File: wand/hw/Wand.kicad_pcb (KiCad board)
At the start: 2 copper layers, 0 parts

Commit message: (WIP) Wand PCB design
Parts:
- added AE1: 2.4GHz 50R, Wand_footprints:ANT_IFA_USB_2.4GHz_50R, F.Cu at (72.2, 25.4)
- added BT1: LiPo, Wand_footprints:Pads_1x02_P2.5, F.Cu at (37.8, 26.1)
- added C1: 10n, Capacitor_SMD:C_0603_1608Metric, F.Cu at (43.4, 31.7)
- added C10: 10n, Capacitor_SMD:C_0402_1005Metric, F.Cu at (61.0, 33.6)
- added C11: 10n, Capacitor_SMD:C_0402_1005Metric, F.Cu at (62.2, 27.0)
- added C12: 33n, Capacitor_SMD:C_0402_1005Metric, F.Cu at (60.4, 26.5)
- added C13: 10p, Capacitor_SMD:C_0402_1005Metric, F.Cu at (64.5, 36.2)
- added C14: 10p, Capacitor_SMD:C_0402_1005Metric, F.Cu at (60.5, 37.2)
- added C15: 1.5p, Capacitor_SMD:C_0402_1005Metric, F.Cu at (68.8, 29.8)
- added C16: 1p, Capacitor_SMD:C_0402_1005Metric, F.Cu at (69.2, 28.4)
- added C17: 2.2n, Capacitor_SMD:C_0402_1005Metric, F.Cu at (68.1, 31.9)
- added C18: 4.7p, Capacitor_SMD:C_0402_1005Metric, F.Cu at (68.1, 30.9)
- added C19: 4.7u, Capacitor_SMD:C_0603_1608Metric, F.Cu at (33.0, 27.6)
- added C2: 4.7u, Capacitor_SMD:C_0603_1608Metric, F.Cu at (46.3, 29.1)
- added C20: 10u, Capacitor_SMD:C_0603_1608Metric, F.Cu at (37.0, 29.5)
- added C3: 4.7u, Capacitor_SMD:C_0603_1608Metric, F.Cu at (47.8, 29.6)
- added C4: 100n, Capacitor_SMD:C_0603_1608Metric, F.Cu at (49.3, 29.6)
- added C5: 100n, Capacitor_SMD:C_0402_1005Metric, F.Cu at (48.7, 45.7)
- added C6: 100n, Capacitor_SMD:C_0402_1005Metric, F.Cu at (51.4, 46.1)
- added C7: 2.2u, Capacitor_SMD:C_0402_1005Metric, F.Cu at (53.2, 46.1)
- added C8: 1n, Capacitor_SMD:C_0603_1608Metric, B.Cu at (42.0, 28.6)
- added C9: 4.7u, Capacitor_SMD:C_0402_1005Metric, F.Cu at (62.2, 26.0)
- added D1: SMBJ5.0A, Diode_SMD:D_SMB, F.Cu at (26.9, 37.4)
- added D2: LED, LED_SMD:LED_0603_1608Metric, F.Cu at (36.7, 34.1)
- added J1: Conn_01x04, Wand_footprints:TestPoints_1x04_P2.0, F.Cu at (52.1, 25.7)
- added J2: Conn_01x08, Connector_PinHeader_1.00mm:PinHeader_1x08_P1.00mm_Vertical, F.Cu at (53.4, 39.0)
- added J3: Conn_01x08, Connector_PinHeader_1.00mm:PinHeader_1x08_P1.00mm_Vertical, F.Cu at (53.4, 41.2)
- added J4: Conn_01x04, Connector_PinHeader_1.00mm:PinHeader_1x04_P1.00mm_Vertical, F.Cu at (46.4, 46.0)
- added J5: USB_C_Receptacle_PowerOnly_6P, Wand_footprints:USB_C_Receptacle, F.Cu at (27.4, 29.8)
- added L1: 8.2n, Capacitor_SMD:C_0402_1005Metric, F.Cu at (65.3, 30.3)
- added L2: 2.7n, Capacitor_SMD:C_0402_1005Metric, F.Cu at (66.4, 31.4)
- added L3: 3.9n, Capacitor_SMD:C_0402_1005Metric, F.Cu at (66.9, 29.8)
- added M1: Motor_DC, Wand_footprints:Pads_1x02_P2.5, B.Cu at (57.0, 37.3)
- added Q1: Si2301, Package_TO_SOT_SMD:SOT-23, F.Cu at (55.5, 36.7)
- added Q2: Si2301, Package_TO_SOT_SMD:SOT-23, B.Cu at (55.9, 34.7)
- added R1: 1.2M, Resistor_SMD:R_0603_1608Metric, F.Cu at (57.6, 25.8)
- added R10: 1k, Resistor_SMD:R_0603_1608Metric, B.Cu at (58.6, 34.6)
- added R11: 5.1k, Resistor_SMD:R_0603_1608Metric, F.Cu at (32.0, 36.4)
- added R12: 5.1k, Resistor_SMD:R_0603_1608Metric, F.Cu at (32.0, 37.9)
- added R13: 2k, Resistor_SMD:R_0603_1608Metric, F.Cu at (33.7, 32.5)
- added R14: 6.8k, Resistor_SMD:R_0603_1608Metric, F.Cu at (33.7, 34.1)
- added R2: 1k, Resistor_SMD:R_0603_1608Metric, F.Cu at (51.4, 36.6)
- added R3: 1k, Resistor_SMD:R_0603_1608Metric, F.Cu at (52.9, 36.6)
- added R4: 1k TBD, Resistor_SMD:R_0603_1608Metric, F.Cu at (46.1, 36.6)
- added R5: 1k TBD, Resistor_SMD:R_0603_1608Metric, F.Cu at (47.6, 36.6)
- added R6: 1k TBD, Resistor_SMD:R_0603_1608Metric, F.Cu at (49.1, 36.6)
- added R7: 3.3M, Resistor_SMD:R_0603_1608Metric, B.Cu at (43.6, 28.6)
- added R8: 100k, Resistor_SMD:R_0603_1608Metric, B.Cu at (42.9, 34.6)
- added R9: 22k, Resistor_SMD:R_0603_1608Metric, F.Cu at (65.3, 26.7)
- added SW1: SW_SPST, Wand_footprints:SPST_1x01_P2.54, F.Cu at (40.0, 33.0)
- added SW2: Vib, Wand_footprints:VibSwitch_JYX-1210-X160, B.Cu at (42.9, 32.0)
- added U1: SPX3819M5-L-3-3, Package_TO_SOT_SMD:SOT-23-5, F.Cu at (43.4, 29.1)
- added U2: STM32G030F6Px, Package_SO:TSSOP-20_4.4x6.5mm_P0.65mm, F.Cu at (53.9, 30.4)
- added U3: BMI270, Wand_footprints:QFN50P300X250X87-14N, F.Cu at (52.1, 43.8)
- added U4: MMC5603NJ, Package_BGA:WLP-4_0.86x0.86mm_P0.4mm, F.Cu at (48.6, 43.8)
- added U5: nRF24L01P, Wand_footprints:QFN-20-P0.5, F.Cu at (62.0, 30.1)
- added U6: LTC4054ES5-4.2, Package_TO_SOT_SMD:TSOT-23-5, F.Cu at (34.1, 30.1)
- added Y1: 16MHz, Crystal:Crystal_SMD_2016-4Pin_2.0x1.6mm, F.Cu at (62.5, 36.4)
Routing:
- net VDD: track 0.00 -> 44.3 mm, vias 0 -> 2
- net GND: track 0.00 -> 38.0 mm, vias 0 -> 35
- net VBUS: track 0.00 -> 24.6 mm
- net VDDSUB: track 0.00 -> 22.3 mm, vias 0 -> 1
- net VIB_TRG: track 0.00 -> 20.7 mm, vias 0 -> 1
- net Net-(SW1-B): track 0.00 -> 15.2 mm
- net SPI2_SCK: track 0.00 -> 15.2 mm, vias 0 -> 1
- net Net-(U2-PB3/PB4/PB5/PB6): track 0.00 -> 14.5 mm, vias 0 -> 2
- net Net-(U2-PB0/PB1/PB2/PA8): track 0.00 -> 13.9 mm, vias 0 -> 2
- net BMI_CS: track 0.00 -> 13.6 mm, vias 0 -> 1
- net VBAT: track 0.00 -> 12.3 mm, vias 0 -> 1
- net Net-(U2-PB7/PB8): track 0.00 -> 12.1 mm, vias 0 -> 2
- net SUB_VDD_G: track 0.00 -> 10.4 mm, vias 0 -> 2
- net Net-(U2-PA12/PA10): track 0.00 -> 10.2 mm
- net Net-(J5-CC1): track 0.00 -> 10.00 mm
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- added copper zone on B.Cu, net GND
- added copper zone on F.Cu, net GND
- added copper zone on B.Cu, net VIB_TRG
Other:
- board outline added: 55 x 22.1 mm

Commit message: Revise wand hardware design
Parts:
- M1: moved to F.Cu
- moved M1 14.0 mm to (43.1, 38.2)
- moved Q2 14.0 mm to (42.0, 35.6)
- moved R10 14.0 mm to (44.7, 35.5)
- moved SW2 2.07 mm to (43.1, 29.9)
- moved C8 2.07 mm to (42.3, 26.6)
- moved R7 2.07 mm to (43.9, 26.6)
- moved R8 2.07 mm to (43.1, 32.6)
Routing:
- net VDD: track 44.3 -> 58.4 mm, vias 2 -> 3
- net MOTOR_G: track 2.02 -> 13.4 mm
- net VIB_TRG: track 20.7 -> 19.6 mm
- net GND: track 38.0 -> 37.0 mm
- net VBAT: track 12.3 -> 13.0 mm
- net Net-(U2-PB0/PB1/PB2/PA8): track 13.9 -> 14.4 mm
- net Net-(M1--): track 3.21 -> 3.59 mm, vias 0 -> 1
- added copper zone on F.Cu, net VDD

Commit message: Revise wand hardware design
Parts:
- added G***: LOGO, LOGO, B.Cu at (75.2, 36.9)
- added G***: LOGO, LOGO, B.Cu at (74.9, 29.9)
- added G***: LOGO, LOGO, B.Cu at (25.4, 37.4)
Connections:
- Q1 pad 2: VDDSUB -> VDD
- Q1 pad 3: VDD -> VDDSUB
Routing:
- net VDDSUB: track 22.3 -> 24.7 mm
- net GND: track 37.0 -> 35.6 mm, vias 35 -> 137
- net VDD: track 58.4 -> 57.4 mm
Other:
- board text added: "23-Cold"
- board text added: "JLCJLCJLCJLC"
- board text added: "Malletwand"
- board text added: "Wand Rev. 2"

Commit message: Revise silkscreen text; submit for fabrication
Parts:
- added G***: LOGO, LOGO, B.Cu at (30.8, 38.6)
- moved G*** 0.23 mm to (75.2, 29.9)
- moved G*** 0.06 mm to (75.3, 37.0)
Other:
- board text removed: "23-Cold"

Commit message: Fix incorrect markings in ECAD files
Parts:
- C5: renamed from C7; value 2.2u -> 100n
- C7: renamed from C5; value 100n -> 2.2u
- M1: value Motor_DC -> Vib
- Q2: value Si2301 -> Si2302
- turned C5 to 180 degrees
- turned C7 to 0 degrees
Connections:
- C5 pad 1: GND -> VDDSUB
- C5 pad 2: VDDSUB -> GND
- C7 pad 1: VDDSUB -> GND
- C7 pad 2: GND -> VDDSUB
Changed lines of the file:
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@@
   )
   (footprint "Capacitor_SMD:C_0402_1005Metric" (layer "F.Cu")
-    (at 48.7 45.7 180)
+    (at 48.7 45.7)
     (descr "Capacitor SMD 0402 (1005 Metric), square (rectangular) end terminal, IPC_7351 nominal, (Body size source: IPC-SM-782 page 76, https://www.pcb-3d.com/wordpress/wp-content/uploads/ipc-sm-782a_amendment_1_and_2.pdf), generated with kicad-footprint-generator")
     (tags "capacitor")
@@
     (property "ki_keywords" "cap capacitor")
     (attr smd)
-    (fp_text reference "C5" (at 0 0 180) (layer "B.SilkS")
+    (fp_text reference "C7" (at 0 0) (layer "B.SilkS")
         (effects (font (size 0.8 0.8) (thickness 0.15)) (justify mirror))
     )
-    (fp_text value "100n" (at 0 1.16) (layer "F.Fab")
+    (fp_text value "2.2u" (at 0 1.16) (layer "F.Fab")
         (effects (font (size 1 1) (thickness 0.15)))
     )
@@
     (fp_line (start 0.5 0.25) (end -0.5 0.25)
       (stroke (width 0.1) (type solid)) (layer "F.Fab"))
-    (pad "1" smd roundrect (at -0.48 0 180) (size 0.56 0.62) (layers "F.Cu" "F.Paste" "F.Mask") (roundrect_rratio 0.25)
-      (net 43 "VDDSUB") (pintype "passive"))
-    (pad "2" smd roundrect (at 0.48 0 180) (size 0.56 0.62) (layers "F.Cu" "F.Paste" "F.Mask") (roundrect_rratio 0.25)
+    (pad "1" smd roundrect (at -0.48 0) (size 0.56 0.62) (layers "F.Cu" "F.Paste" "F.Mask") (roundrect_rratio 0.25)
       (net 2 "GND") (pintype "passive"))
+    (pad "2" smd roundrect (at 0.48 0) (size 0.56 0.62) (layers "F.Cu" "F.Paste" "F.Mask") (roundrect_rratio 0.25)
+      (net 43 "VDDSUB") (pintype "passive"))
     (model "${KICAD6_3DMODEL_DIR}/Capacitor_SMD.3dshapes/C_0402_1005Metric.wrl"
       (offset (xyz 0 0 0))
@@
         (effects (font (size 0.8 0.8) (thickness 0.15)))
     )
-    (fp_text value "Motor_DC" (at 0 1 180 unlocked) (layer "F.Fab")
+    (fp_text value "Vib" (at 0 1 180 unlocked) (layer "F.Fab")
         (effects (font (size 1 1) (thickness 0.15)))
     )
@@
   )
   (footprint "Capacitor_SMD:C_0402_1005Metric" (layer "F.Cu")
-    (at 53.2 46.15)
+    (at 53.2 46.15 180)
     (descr "Capacitor SMD 0402 (1005 Metric), square (rectangular) end terminal, IPC_7351 nominal, (Body size source: IPC-SM-782 page 76, https://www.pcb-3d.com/wordpress/wp-content/uploads/ipc-sm-782a_amendment_1_and_2.pdf), generated with kicad-footprint-generator")
     (tags "capacitor")
@@
     (property "ki_keywords" "cap capacitor")
     (attr smd)
-    (fp_text reference "C7" (at 0 0.05) (layer "B.SilkS")
+    (fp_text reference "C5" (at 0 0.05) (layer "B.SilkS")
         (effects (font (size 0.8 0.8) (thickness 0.15)) (justify mirror))
     )
-    (fp_text value "2.2u" (at 0 1.16) (layer "F.Fab")
+    (fp_text value "100n" (at 0 1.16) (layer "F.Fab")
         (effects (font (size 1 1) (thickness 0.15)))
     )
@@
     (fp_line (start 0.5 0.25) (end -0.5 0.25)
       (stroke (width 0.1) (type solid)) (layer "F.Fab"))
-    (pad "1" smd roundrect (at -0.48 0) (size 0.56 0.62) (layers "F.Cu" "F.Paste" "F.Mask") (roundrect_rratio 0.25)
-      (net 2 "GND") (pintype "passive"))
-    (pad "2" smd roundrect (at 0.48 0) (size 0.56 0.62) (layers "F.Cu" "F.Paste" "F.Mask") (roundrect_rratio 0.25)
+    (pad "1" smd roundrect (at -0.48 0 180) (size 0.56 0.62) (layers "F.Cu" "F.Paste" "F.Mask") (roundrect_rratio 0.25)
       (net 43 "VDDSUB") (pintype "passive"))
+    (pad "2" smd roundrect (at 0.48 0 180) (size 0.56 0.62) (layers "F.Cu" "F.Paste" "F.Mask") (roundrect_rratio 0.25)
+      (net 2 "GND") (pintype "passive"))
     (model "${KICAD6_3DMODEL_DIR}/Capacitor_SMD.3dshapes/C_0402_1005Metric.wrl"
       (offset (xyz 0 0 0))
@@
         (effects (font (size 0.8 0.8) (thickness 0.15)) (justify mirror))
     )
-    (fp_text value "Si2301" (at 0 -2.4) (layer "B.Fab")
+    (fp_text value "Si2302" (at 0 -2.4) (layer "B.Fab")
         (effects (font (size 1 1) (thickness 0.15)) (justify mirror))
     )

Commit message: Revise central module hardware design
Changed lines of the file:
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@@
   (segment (start 46.4 41.165) (end 46.4 42.9875) (width 0.2) (layer "B.Cu") (net 17))
   (segment (start 46.4 42.9875) (end 46.415 43.0025) (width 0.2) (layer "B.Cu") (net 17))
-  (segment (start 65.13 30.78) (end 64.92 30.57) (width 0.25) (layer "F.Cu") (net 18))
+  (segment (start 64.97 30.57) (end 63.889444 30.57) (width 0.25) (layer "F.Cu") (net 18))
+  (segment (start 65.18 30.78) (end 64.97 30.57) (width 0.25) (layer "F.Cu") (net 18))
   (segment (start 66.261944 30.78) (end 65.301944 30.78) (width 0.5) (layer "F.Cu") (net 18))
   (segment (start 66.401944 30.92) (end 66.261944 30.78) (width 0.5) (layer "F.Cu") (net 18))
-  (segment (start 64.92 30.57) (end 63.889444 30.57) (width 0.25) (layer "F.Cu") (net 18))
-  (segment (start 65.301944 30.78) (end 65.13 30.78) (width 0.25) (layer "F.Cu") (net 18))
+  (segment (start 65.301944 30.78) (end 65.18 30.78) (width 0.25) (layer "F.Cu") (net 18))
   (segment (start 65.301944 29.82) (end 66.401944 29.82) (width 0.5) (layer "F.Cu") (net 19))
   (segment (start 63.889444 30.07) (end 64.93 30.07) (width 0.25) (layer "F.Cu") (net 19))
@@
       1ae7fdbc-dc24-4dbc-8335-f601929143ab
       1ce4cfef-1acf-4f91-86d6-219b9e688972
-      2432a2b4-0238-4f92-a335-b42a5372838a
       260ba61f-c53f-48ba-97d8-69aef29b574b
       2cf0ce3f-27a7-4e31-857d-8bf2352fe25a
@@
       72d9d2f3-21e0-41fd-b522-1e49beed2d54
       77eeec9e-5196-4557-89b9-e1408de4fdab
-      7a6aa5ce-2b3f-4bca-8534-bc4ae8b043ef
       7f215527-fd74-4f46-9b45-7cf1f4273f97
       857b36a3-1857-4be7-9e62-4bf93613146f
@@
       aac73ff9-7c2a-4b0f-9ba8-7982bb59e4be
       aad41cf6-45bb-4206-82e5-5b1ebcf1a0d6
-      ae21d5ae-8dcd-4ffc-834b-fdd882701453
       b2763c0c-782e-4c52-9595-57bb1cbb5d06
       b5bc7fd7-ff48-4584-966c-9b43adf147ac
@@
       c4047f87-c49d-42de-815b-7f8c8990124c
       c65dcfb7-c88e-4f35-9369-7d2430eff168
-      c6faa4c7-a161-4178-9c94-144fc49306f4
-      c731ba39-48a5-466a-8692-24d08eaf518a
       c8ca79a4-6873-4674-a006-0a93bd8d45c7
       cafe9b43-99fd-42e9-9d24-f6b17f625389
-      cb68e2a9-ec28-4d02-927f-89dc716e6524
       cc473c23-7092-4962-b037-7fc8ef7d2fbd
       d1a13572-b16f-4866-a7e1-2e4a19a35828

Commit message: Revise wand hardware design
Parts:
- added D3: MBR0530, Diode_SMD:D_SOD-123, F.Cu at (37.5, 35.8)
- added R11: 100k, Resistor_SMD:R_0603_1608Metric, F.Cu at (43.4, 34.5)
- C8, Q2, R10, R7, R8, SW2: moved to F.Cu
- J4: footprint Connector_PinHeader_1.00mm:PinHeader_1x04_P1.00mm_Vertical -> Connector_PinHeader_1.27mm:PinHeader_1x04_P1.27mm_Vertical
- moved SW1 6.10 mm to (33.9, 33.0)
- moved BT1 6.00 mm to (31.8, 26.1)
- moved D2 6.00 mm to (30.7, 34.1)
- moved R14 6.00 mm to (27.7, 32.5)
- moved R15 6.00 mm to (27.7, 34.1)
- moved C1 6.00 mm to (37.4, 31.7)
- moved C2 6.00 mm to (40.3, 29.1)
- moved C20 6.00 mm to (31.0, 29.5)
- moved D1 6.00 mm to (20.9, 37.4)
- moved J5 6.00 mm to (21.4, 29.8)
- moved R12 6.00 mm to (26.0, 36.4)
- moved R13 6.00 mm to (26.0, 37.9)
- moved U1 6.00 mm to (37.4, 29.1)
- moved U6 6.00 mm to (28.1, 30.1)
- moved C19 6.00 mm to (27.1, 27.6)
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- renumbered R11 to R12, R12 to R13, R13 to R14, R14 to R15
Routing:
- net VDD: track 57.4 -> 69.4 mm
- net VDDSUB: track 24.7 -> 30.8 mm
- net Net-(D3-A): track 3.59 -> 9.55 mm, vias 1 -> 0
- net VBAT: track 13.0 -> 18.8 mm, vias 1 -> 0
- net LED_B: track 5.67 -> 10.7 mm
- net LED_G: track 7.07 -> 11.1 mm
- net Net-(AE1-Pad1): track 5.31 -> 8.45 mm
- net VIB_TRG: track 19.6 -> 22.4 mm, vias 1 -> 2
- net SPI2_MOSI: track 5.31 -> 7.88 mm
- net LED_R: track 9.70 -> 11.9 mm
- net MOTOR_G: track 13.4 -> 15.1 mm, vias 1 -> 2
- net BMI_CS: track 13.6 -> 14.4 mm
- net SPI2_SCK: track 15.2 -> 16.0 mm
- net Net-(Q2-G): track 2.64 -> 1.88 mm
- net GND: track 35.6 -> 36.2 mm, vias 137 -> 157
- removed copper zone on B.Cu, net VIB_TRG
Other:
- board size 55 x 22.1 mm -> 63.2 x 22.5 mm
- board text added: "Wand Rev. 3"
- board text removed: "Wand Rev. 2"

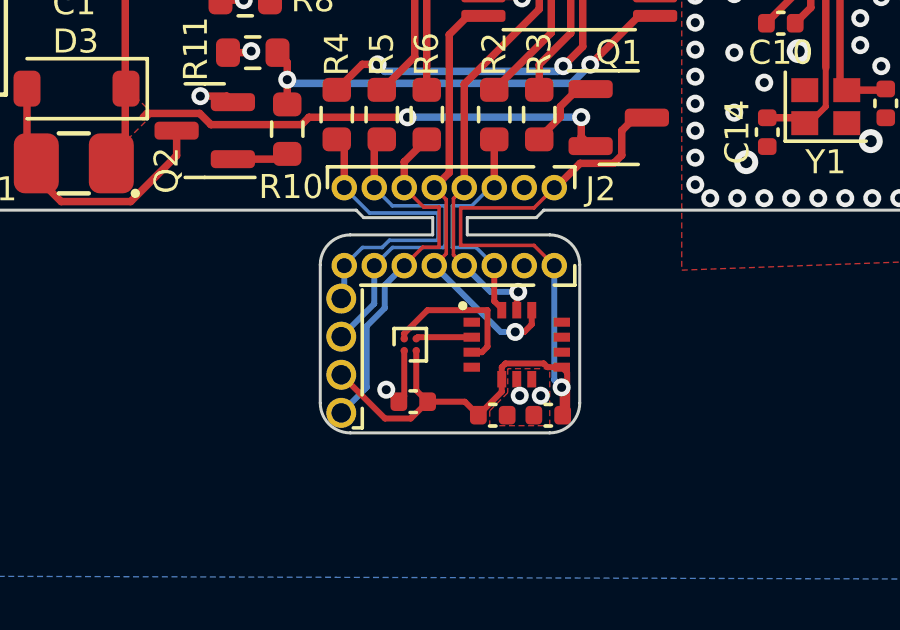
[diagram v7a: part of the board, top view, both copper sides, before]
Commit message: Revise wand PCB as per fab. clearance requirements
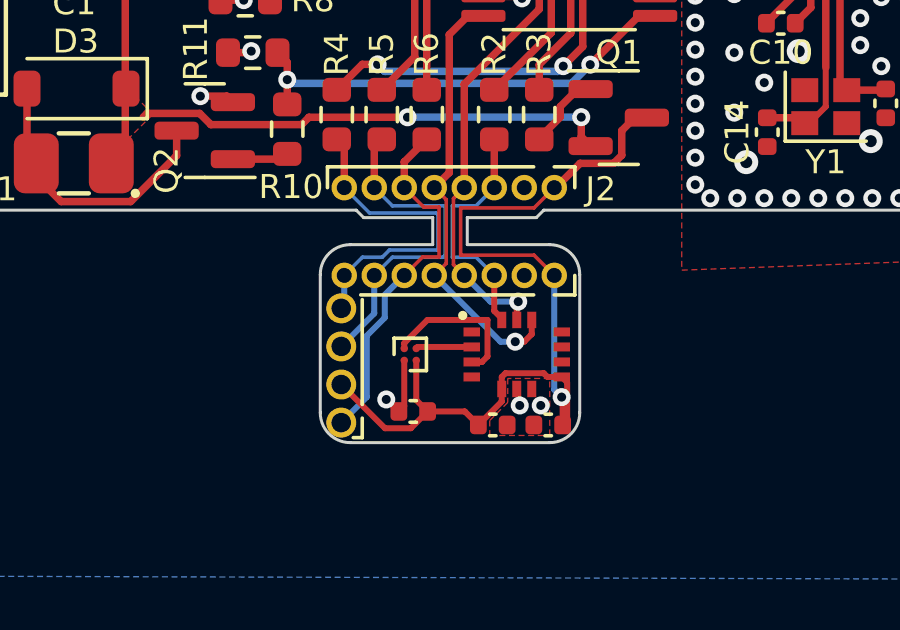
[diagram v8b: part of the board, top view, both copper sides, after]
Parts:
- moved C5 0.33 mm to (53.2, 47.0)
- moved C6 0.33 mm to (51.4, 47.0)
- moved J3 0.33 mm to (53.4, 42.0)
- moved J4 0.33 mm to (46.3, 46.9)
- moved U3 0.33 mm to (52.1, 44.6)
- moved U4 0.33 mm to (48.6, 44.6)
- moved C7 0.32 mm to (48.7, 46.5)
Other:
- board size 63.2 x 22.5 mm -> 63.2 x 22.8 mm
